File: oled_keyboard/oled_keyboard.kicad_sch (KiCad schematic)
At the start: 115 parts, among them J1 Conn_01x20_Socket, J10 Conn_01x20_Socket, J11 Conn_01x20_Socket, J12 Conn_01x20_Socket, J2 Conn_01x20_Socket, J3 Conn_01x20_Socket, J4 Conn_01x20_Socket, J5 Conn_01x20_Socket, J6 Conn_01x20_Socket, J7 Conn_01x20_Socket, J8 Conn_01x20_Socket, J9 Conn_01x20_Socket, SW1 SW_Push, SW10 SW_Push, SW11 SW_Push, SW12 SW_Push, SW2 SW_Push, SW3 SW_Push, SW4 SW_Push, SW5 SW_Push, SW6 SW_Push, SW7 SW_Push, SW8 SW_Push, SW9 SW_Push, U1 TPS61088RHLR

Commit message: routing in progress
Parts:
- added NT1: NetTie_2, NetTie:NetTie-2_SMD_Pad0.5mm, symbol Device:NetTie_2
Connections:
- net SCLK is gone; now on net SCK: J1.11 (Pin_11), J10.11 (Pin_11), J11.11 (Pin_11), J12.11 (Pin_11), J2.11 (Pin_11), J3.11 (Pin_11), J4.11 (Pin_11), J5.11 (Pin_11), J6.11 (Pin_11), J7.11 (Pin_11), J8.11 (Pin_11), J9.11 (Pin_11)
- net SDIN is gone; now on net MOSI: J1.10 (Pin_10), J10.10 (Pin_10), J11.10 (Pin_10), J12.10 (Pin_10), J2.10 (Pin_10), J3.10 (Pin_10), J4.10 (Pin_10), J5.10 (Pin_10), J6.10 (Pin_10), J7.10 (Pin_10), J8.10 (Pin_10), J9.10 (Pin_10)
- net VUSB is gone; now on net VBUS: L1.1
- net AGND: now also NT1.1; no longer A1.13 (GND), A1.18 (GND), A1.23 (GND), A1.28 (GND), A1.3 (GND), A1.33 (AGND), A1.37 (3V3_EN), A1.38 (GND), A1.8 (GND), C1.2, C10.1, C11.1, C14.2, C15.2, C16.2, C17.2, C18.2, C19.2, C2.2, C20.2, C21.2, C22.2, C23.2, C24.2, C25.2, C26.2, C27.2, C28.2, C29.2, C3.2, C30.2, C31.2, C32.2, C33.2, C34.2, C35.2, C36.2, C37.2, C38.2, C39.2, C4.2, C40.2, C41.2, C42.2, C43.2, C44.2, C45.2, C46.2, C47.2, C48.2, C49.2, C5.2, C50.2, C51.2, C52.2, C53.2, C54.2, C55.2, C56.2, C57.2, C58.2, C59.2, C6.2, R1.2, R10.2, R11.2, R12.2, R13.2, R14.2, R15.2, R16.2, R17.2, R2.2, R3.2, R9.2, U1.21 (PGND), U1.22 (PGND), U1.23 (PGND), U1.24 (PGND), U1.25 (PGND), U1.26 (PGND), U1.27 (PGND), U1.28 (PGND), U1.29 (PGND)
- net COL1: now also A1.5 (GPIO3); no longer A1.6 (GPIO4)
- net COL2: now also A1.4 (GPIO2); no longer A1.7 (GPIO5)
- net COL3: now also A1.2 (GPIO1); no longer A1.9 (GPIO6)
- net CS1: now also A1.6 (GPIO4); no longer A1.10 (GPIO7)
- net CS10: now also A1.17 (GPIO13); no longer A1.26 (GPIO20)
- net CS11: now also A1.19 (GPIO14); no longer A1.27 (GPIO21)
- net CS12: now also A1.20 (GPIO15); no longer A1.29 (GPIO22)
- net CS2: now also A1.7 (GPIO5); no longer A1.11 (GPIO8)
- net CS3: now also A1.9 (GPIO6); no longer A1.12 (GPIO9)
- net CS4: now also A1.10 (GPIO7); no longer A1.14 (GPIO10)
- net CS5: now also A1.11 (GPIO8); no longer A1.15 (GPIO11)
- net CS6: now also A1.12 (GPIO9); no longer A1.16 (GPIO12)
- net CS7: now also A1.14 (GPIO10); no longer A1.17 (GPIO13)
- net CS8: now also A1.15 (GPIO11); no longer A1.19 (GPIO14)
- net CS9: now also A1.16 (GPIO12); no longer A1.20 (GPIO15)
- net DC: now also A1.31 (GPIO26_ADC0)
- net RES: now also A1.32 (GPIO27_ADC1)
- net ROW2: now also A1.27 (GPIO21); no longer A1.2 (GPIO1)
- net ROW3: now also A1.26 (GPIO20); no longer A1.4 (GPIO2)
- net ROW4: now also A1.22 (GPIO17); no longer A1.5 (GPIO3)
- new net GND: A1.13 (GND), A1.18 (GND), A1.23 (GND), A1.28 (GND), A1.3 (GND), A1.33 (AGND), A1.37 (3V3_EN), A1.38 (GND), A1.8 (GND), C1.2, C10.1, C11.1, C14.2, C15.2, C16.2, C17.2, C18.2, C19.2, C2.2, C20.2, C21.2, C22.2, C23.2, C24.2, C25.2, C26.2, C27.2, C28.2, C29.2, C3.2, C30.2, C31.2, C32.2, C33.2, C34.2, C35.2, C36.2, C37.2, C38.2, C39.2, C4.2, C40.2, C41.2, C42.2, C43.2, C44.2, C45.2, C46.2, C47.2, C48.2, C49.2, C5.2, C50.2, C51.2, C52.2, C53.2, C54.2, C55.2, C56.2, C57.2, C58.2, C59.2, C6.2, NT1.2, R1.2, R10.2, R11.2, R12.2, R13.2, R14.2, R15.2, R16.2, R17.2, R2.2, R3.2, R9.2, U1.21 (PGND), U1.22 (PGND), U1.23 (PGND), U1.24 (PGND), U1.25 (PGND), U1.26 (PGND), U1.27 (PGND), U1.28 (PGND), U1.29 (PGND)

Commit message: routing ok. added gitignore
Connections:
- net VOUT is gone; now on net VCC: C14.1, C15.1, C16.1, C6.1, R5.2, U1.14 (VOUT_16), U1.15 (VOUT_14), U1.16 (VOUT_15)
- no-connect marks 0 -> 135

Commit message: added test points
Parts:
- added TP1, TP2, TP3, TP4, TP5, TP6, TP7: TestPoint, TestPoint:TestPoint_Pad_D2.5mm, symbol Connector:TestPoint
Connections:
- net DC: now also TP6.1
- net GND: now also TP3.1
- net MOSI: now also TP4.1
- net RES: now also TP7.1
- net SCK: now also TP5.1
- net VBUS: now also TP2.1
- net VCC: now also TP1.1

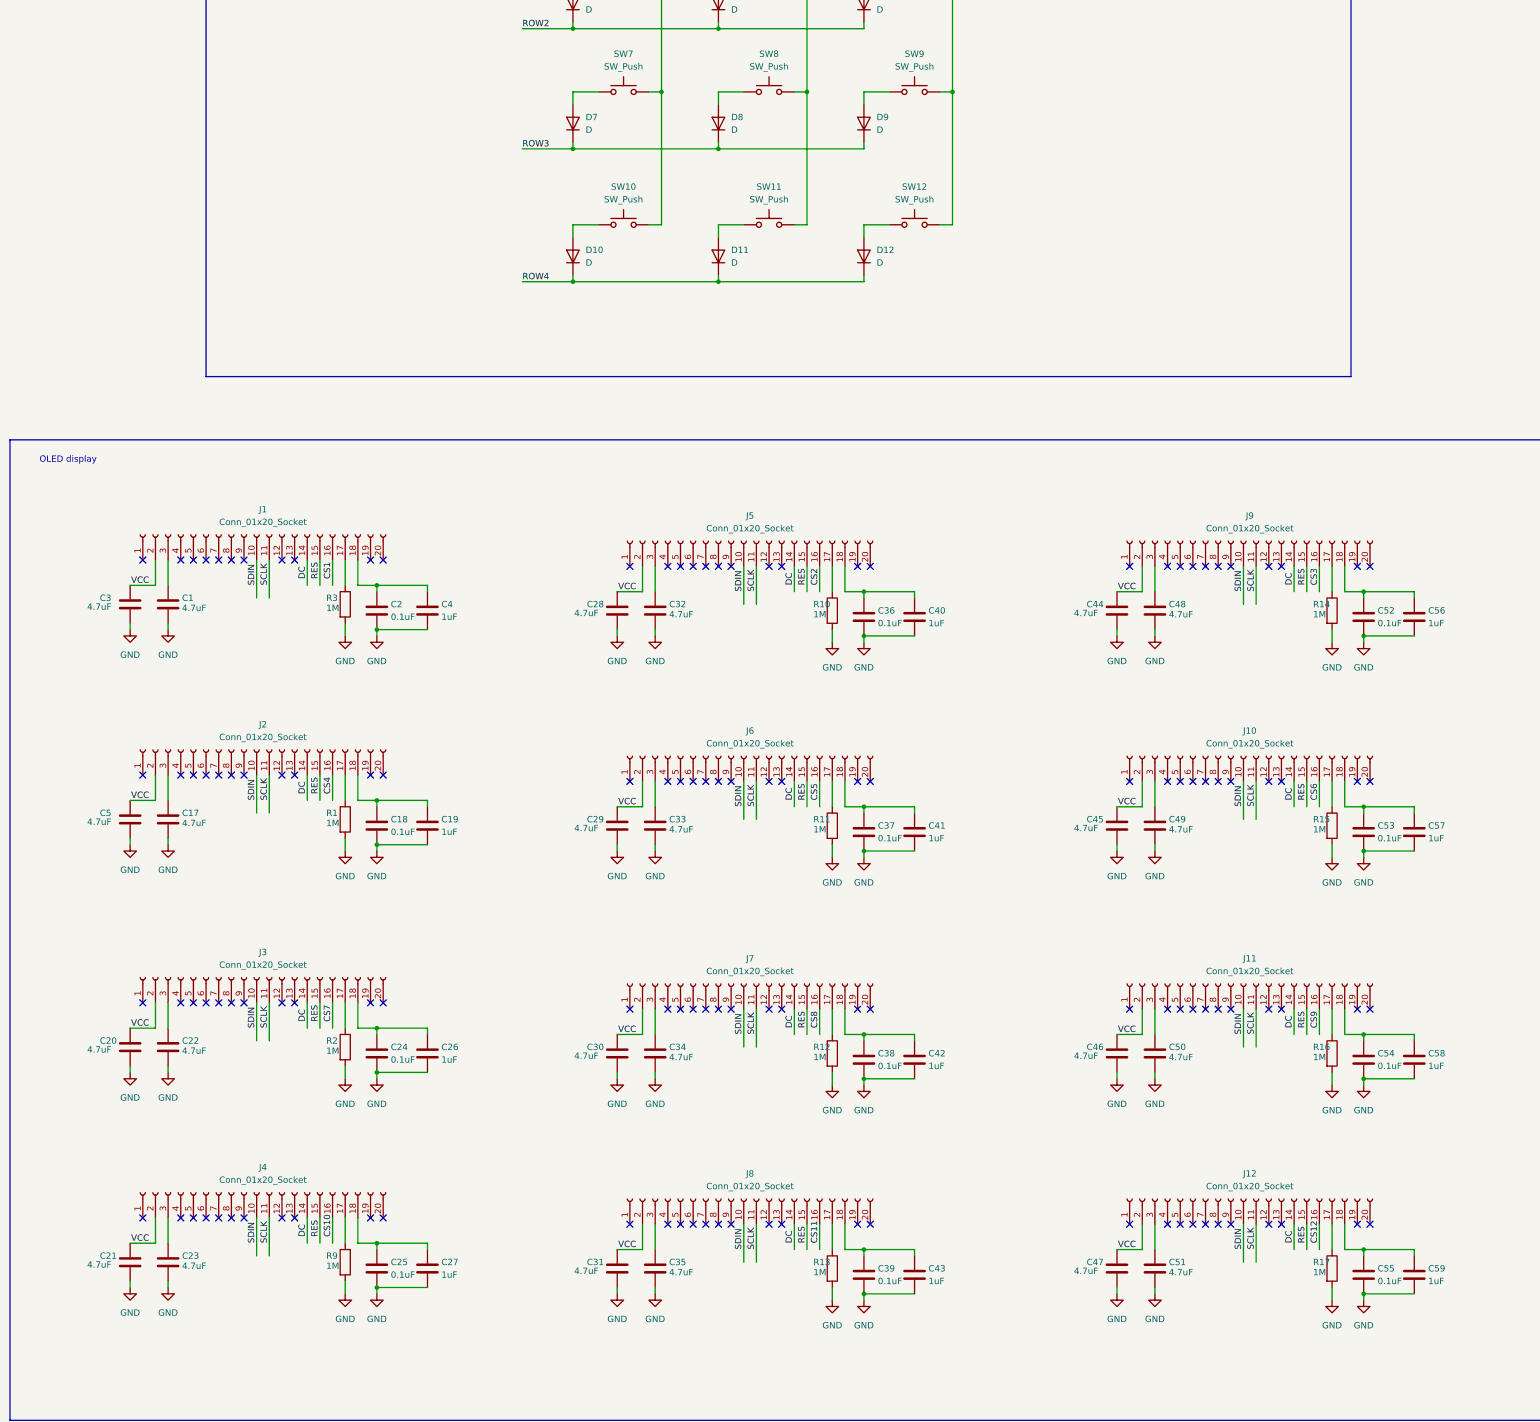
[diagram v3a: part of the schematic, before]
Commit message: chged to 9 oled. fixed pin inversion issue
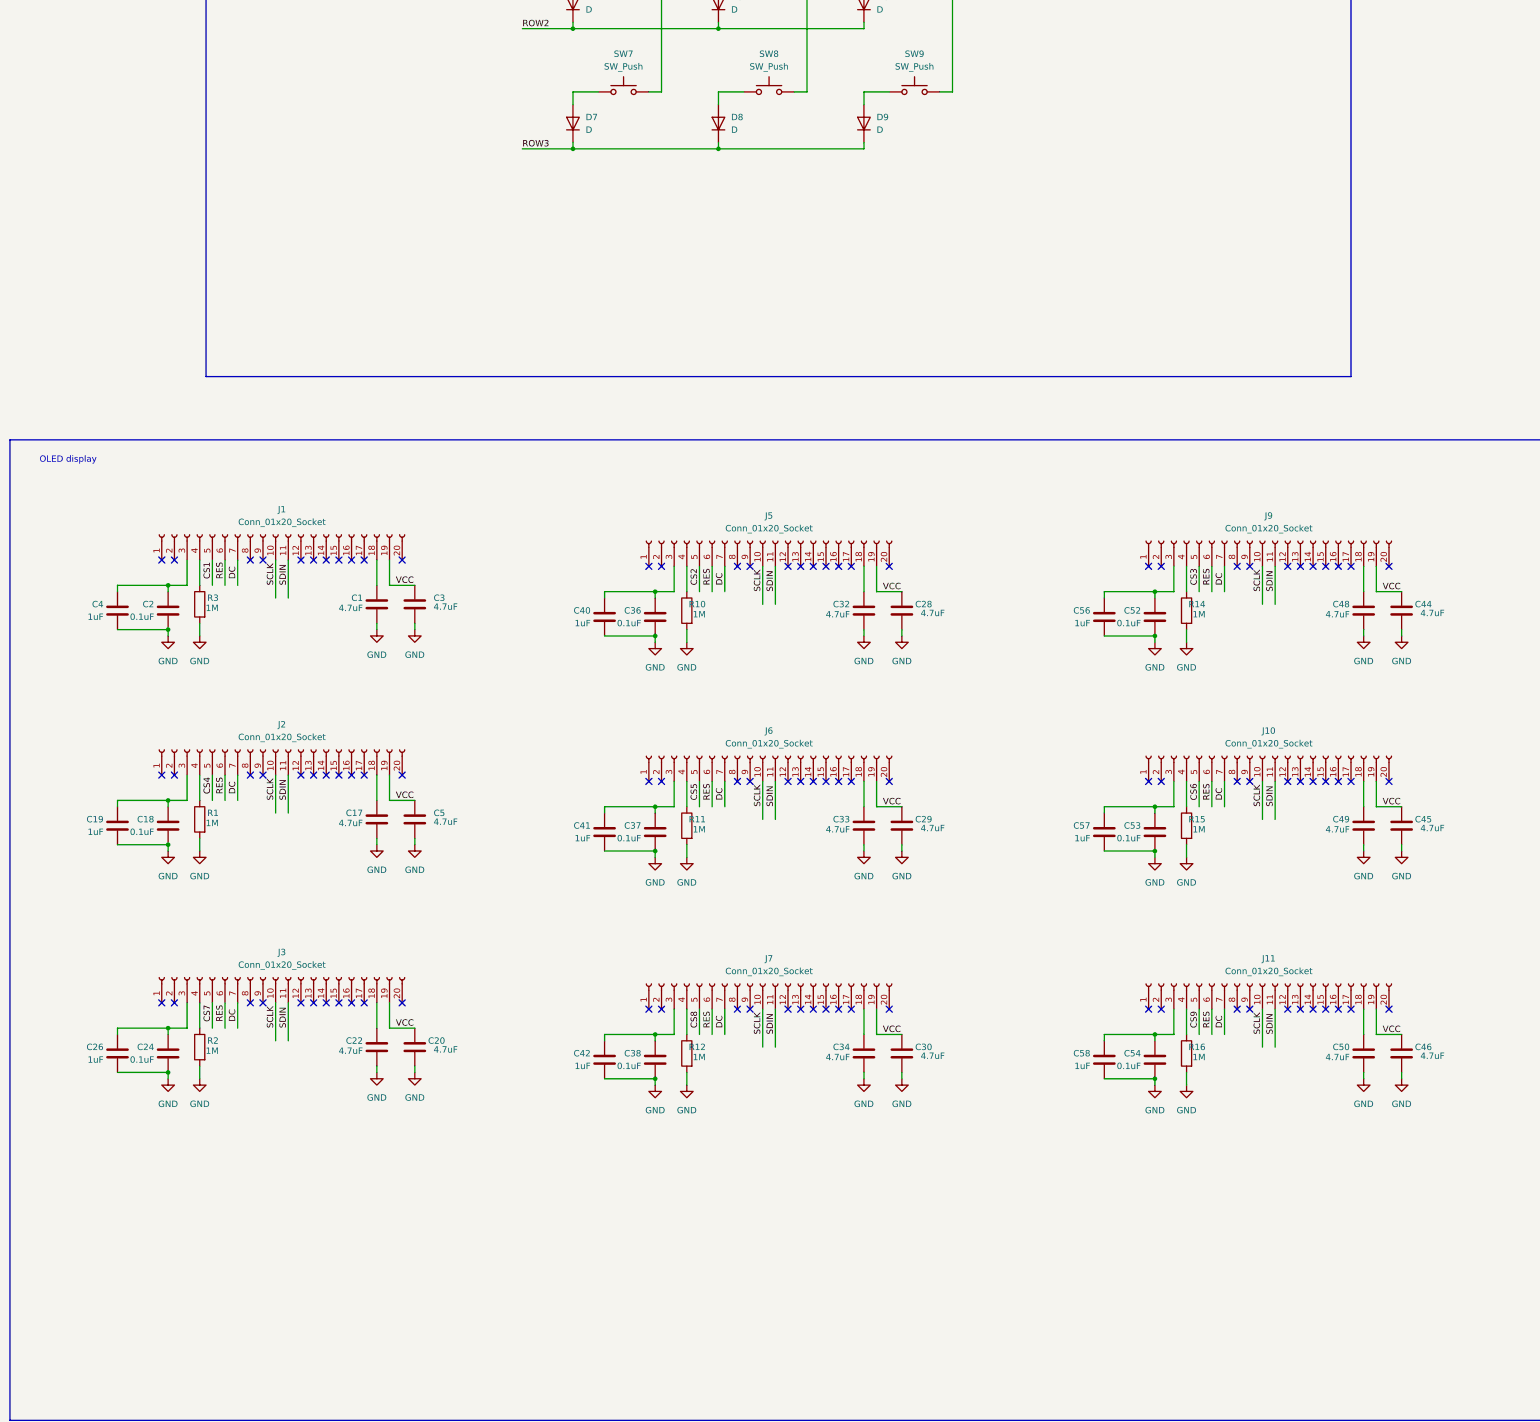
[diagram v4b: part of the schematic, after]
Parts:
- removed C21, C23, C31, C35, C47, C51: 4.7uF, Capacitor_SMD:C_0603_1608Metric, symbol Device:C
- removed C25, C39, C55: 0.1uF, Capacitor_SMD:C_0603_1608Metric, symbol Device:C
- removed C27, C43, C59: 1uF, Capacitor_SMD:C_0603_1608Metric, symbol Device:C
- removed D10, D11, D12: D, Diode_SMD:D_SOD-123F, symbol Device:D
- removed J12, J4, J8: Conn_01x20_Socket, 20p_connector:HRS_TF31-20S-0.5SH_800_, symbol Connector:Conn_01x20_Socket
- removed R13, R17, R9: 1M, Resistor_SMD:R_0603_1608Metric, symbol Device:R
- removed SW10, SW11, SW12: SW_Push, Switch_Keyboard_Kailh:SW_Kailh_Choc_V1V2, symbol Switch:SW_Push
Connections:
- net CS1: now also J1.5 (Pin_5); no longer J1.16 (Pin_16)
- net CS2: now also J5.5 (Pin_5); no longer J5.16 (Pin_16)
- net CS3: now also J9.5 (Pin_5); no longer J9.16 (Pin_16)
- net CS4: now also J2.5 (Pin_5); no longer J2.16 (Pin_16)
- net CS5: now also J6.5 (Pin_5); no longer J6.16 (Pin_16)
- net CS6: now also J10.5 (Pin_5); no longer J10.16 (Pin_16)
- net CS7: now also J3.5 (Pin_5); no longer J3.16 (Pin_16)
- net CS8: now also J7.5 (Pin_5); no longer J7.16 (Pin_16)
- net CS9: now also J11.5 (Pin_5); no longer J11.16 (Pin_16)
- net DC: now also J1.7 (Pin_7), J10.7 (Pin_7), J11.7 (Pin_7), J2.7 (Pin_7), J3.7 (Pin_7), J5.7 (Pin_7), J6.7 (Pin_7), J7.7 (Pin_7), J9.7 (Pin_7); no longer J1.14 (Pin_14), J10.14 (Pin_14), J11.14 (Pin_14), J2.14 (Pin_14), J3.14 (Pin_14), J5.14 (Pin_14), J6.14 (Pin_14), J7.14 (Pin_14), J9.14 (Pin_14)
- net MOSI: now also J1.11 (Pin_11), J10.11 (Pin_11), J11.11 (Pin_11), J2.11 (Pin_11), J3.11 (Pin_11), J5.11 (Pin_11), J6.11 (Pin_11), J7.11 (Pin_11), J9.11 (Pin_11); no longer J1.10 (Pin_10), J10.10 (Pin_10), J11.10 (Pin_10), J2.10 (Pin_10), J3.10 (Pin_10), J5.10 (Pin_10), J6.10 (Pin_10), J7.10 (Pin_10), J9.10 (Pin_10)
- net RES: now also J1.6 (Pin_6), J10.6 (Pin_6), J11.6 (Pin_6), J2.6 (Pin_6), J3.6 (Pin_6), J5.6 (Pin_6), J6.6 (Pin_6), J7.6 (Pin_6), J9.6 (Pin_6); no longer J1.15 (Pin_15), J10.15 (Pin_15), J11.15 (Pin_15), J2.15 (Pin_15), J3.15 (Pin_15), J5.15 (Pin_15), J6.15 (Pin_15), J7.15 (Pin_15), J9.15 (Pin_15)
- net SCK: now also J1.10 (Pin_10), J10.10 (Pin_10), J11.10 (Pin_10), J2.10 (Pin_10), J3.10 (Pin_10), J5.10 (Pin_10), J6.10 (Pin_10), J7.10 (Pin_10), J9.10 (Pin_10); no longer J1.11 (Pin_11), J10.11 (Pin_11), J11.11 (Pin_11), J2.11 (Pin_11), J3.11 (Pin_11), J5.11 (Pin_11), J6.11 (Pin_11), J7.11 (Pin_11), J9.11 (Pin_11)
- net VCC: now also J1.19 (Pin_19), J10.19 (Pin_19), J11.19 (Pin_19), J2.19 (Pin_19), J3.19 (Pin_19), J5.19 (Pin_19), J6.19 (Pin_19), J7.19 (Pin_19), J9.19 (Pin_19); no longer J1.2 (Pin_2), J10.2 (Pin_2), J11.2 (Pin_2), J2.2 (Pin_2), J3.2 (Pin_2), J5.2 (Pin_2), J6.2 (Pin_2), J7.2 (Pin_2), J9.2 (Pin_2)
- net at R16.1: now also J11.4 (Pin_4); no longer J11.17 (Pin_17)
- net at J9.17 (Pin_17): no longer R14.1
- net at C52.1, C56.1: now also J9.3 (Pin_3); no longer J9.18 (Pin_18)
- net at C48.1: now also J9.18 (Pin_18); no longer J9.3 (Pin_3)
- net at J9.4 (Pin_4): now also R14.1
- net at C34.1: now also J7.18 (Pin_18); no longer J7.3 (Pin_3)
- net at C37.1, C41.1: now also J6.3 (Pin_3); no longer J6.18 (Pin_18)
- net at C18.1, C19.1: now also J2.3 (Pin_3); no longer J2.18 (Pin_18)
- net at J2.17 (Pin_17): no longer R1.1
- net at C17.1: now also J2.18 (Pin_18); no longer J2.3 (Pin_3)
- net at J2.4 (Pin_4): now also R1.1
- net at C38.1, C42.1: now also J7.3 (Pin_3); no longer J7.18 (Pin_18)
- net at C36.1, C40.1: now also J5.3 (Pin_3); no longer J5.18 (Pin_18)
- net at C53.1, C57.1: now also J10.3 (Pin_3); no longer J10.18 (Pin_18)
- net at J10.17 (Pin_17): no longer R15.1
- net at C49.1: now also J10.18 (Pin_18); no longer J10.3 (Pin_3)
- net at J10.4 (Pin_4): now also R15.1
- net at R2.1: now also J3.4 (Pin_4); no longer J3.17 (Pin_17)
- net at C24.1, C26.1: now also J3.3 (Pin_3); no longer J3.18 (Pin_18)
- net at C22.1: now also J3.18 (Pin_18); no longer J3.3 (Pin_3)
- net at R10.1: now also J5.4 (Pin_4); no longer J5.17 (Pin_17)
- net at C32.1: now also J5.18 (Pin_18); no longer J5.3 (Pin_3)
- net at C2.1, C4.1: now also J1.3 (Pin_3); no longer J1.18 (Pin_18)
- net at C54.1, C58.1: now also J11.3 (Pin_3); no longer J11.18 (Pin_18)
- net at C50.1: now also J11.18 (Pin_18); no longer J11.3 (Pin_3)
- net at R3.1: now also J1.4 (Pin_4); no longer J1.17 (Pin_17)
- net at C1.1: now also J1.18 (Pin_18); no longer J1.3 (Pin_3)
- net at R11.1: now also J6.4 (Pin_4); no longer J6.17 (Pin_17)
- net at C33.1: now also J6.18 (Pin_18); no longer J6.3 (Pin_3)
- net at J7.17 (Pin_17): no longer R12.1
- net at J7.4 (Pin_4): now also R12.1
- no-connect marks 135 -> 102
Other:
- moved on the sheet: C1, C17, C18, C19, C2, C20, C22, C24, C26, C28, C29, C3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

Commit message: optimized key layout
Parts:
- added C21, C31, C47: 1uF, Capacitor_SMD:C_0603_1608Metric, symbol Device:C
- added C23, C35, C51: 0.1uF, Capacitor_SMD:C_0603_1608Metric, symbol Device:C
- added C25, C27, C39, C43, C55, C59: 4.7uF, Capacitor_SMD:C_0603_1608Metric, symbol Device:C
- added D10, D11, D12: D, Diode_SMD:D_SOD-123F, symbol Device:D
- added J12, J4, J8: Conn_01x20_Socket, 20pin_connector:HRS_TF31-20S-0.5SH_800_, symbol Connector:Conn_01x20_Socket
- added R13, R17, R9: 1M, Resistor_SMD:R_0603_1608Metric, symbol Device:R
- added SW10, SW11, SW12: SW_Push, keyboard_custom:SW_Kailh_Choc_V1V2, symbol Switch:SW_Push
- added TP8: TestPoint, TestPoint:TestPoint_Pad_D2.5mm, symbol Connector:TestPoint
- J1, J10, J11, J2, J3, J5, J6, J7, J9: footprint 20p_connector:HRS_TF31-20S-0.5SH_800_ -> 20pin_connector:HRS_TF31-20S-0.5SH_800_
- SW1, SW2, SW3, SW4, SW5, SW6, SW7, SW8, SW9: footprint Switch_Keyboard_Kailh:SW_Kailh_Choc_V1V2 -> keyboard_custom:SW_Kailh_Choc_V1V2
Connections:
- net COL1: now also SW10.2
- net COL2: now also A1.2 (GPIO1), SW11.2; no longer A1.4 (GPIO2)
- net COL3: now also A1.1 (GPIO0), SW12.2; no longer A1.2 (GPIO1)
- net CS10: now also J4.5 (Pin_5)
- net CS11: now also J8.5 (Pin_5)
- net CS12: now also J12.5 (Pin_5)
- net DC: now also J12.7 (Pin_7), J4.7 (Pin_7), J8.7 (Pin_7)
- net GND: now also C21.2, C23.2, C25.2, C27.2, C31.2, C35.2, C39.2, C43.2, C47.2, C51.2, C55.2, C59.2, R13.2, R17.2, R9.2, TP8.1
- net MOSI: now also J12.11 (Pin_11), J4.11 (Pin_11), J8.11 (Pin_11)
- net RES: now also J12.6 (Pin_6), J4.6 (Pin_6), J8.6 (Pin_6)
- net ROW1: now also A1.4 (GPIO2); no longer A1.1 (GPIO0)
- net ROW4: now also D10.1 (K), D11.1 (K), D12.1 (K)
- net SCK: now also J12.10 (Pin_10), J4.10 (Pin_10), J8.10 (Pin_10)
- net VCC: now also C27.1, C43.1, C59.1, J12.19 (Pin_19), J4.19 (Pin_19), J8.19 (Pin_19)
- new net: C21.1, C23.1, J4.3 (Pin_3)
- new net: D12.2 (A), SW12.1
- new net: C25.1, J4.18 (Pin_18)
- new net: J4.4 (Pin_4), R9.1
- new net: D11.2 (A), SW11.1
- new net: J12.4 (Pin_4), R17.1
- new net: D10.2 (A), SW10.1
- new net: C31.1, C35.1, J8.3 (Pin_3)
- new net: C39.1, J8.18 (Pin_18)
- new net: J8.4 (Pin_4), R13.1
- new net: C55.1, J12.18 (Pin_18)
- new net: C47.1, C51.1, J12.3 (Pin_3)
- no-connect marks 102 -> 135

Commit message: v3.0
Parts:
- added R18, R19: 33R, Resistor_SMD:R_0603_1608Metric, symbol Device:R
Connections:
- net MOSI: now also R19.2; no longer J1.11 (Pin_11), J10.11 (Pin_11), J11.11 (Pin_11), J12.11 (Pin_11), J2.11 (Pin_11), J3.11 (Pin_11), J4.11 (Pin_11), J5.11 (Pin_11), J6.11 (Pin_11), J7.11 (Pin_11), J8.11 (Pin_11), J9.11 (Pin_11)
- net SCK: now also R18.2; no longer J1.10 (Pin_10), J10.10 (Pin_10), J11.10 (Pin_10), J12.10 (Pin_10), J2.10 (Pin_10), J3.10 (Pin_10), J4.10 (Pin_10), J5.10 (Pin_10), J6.10 (Pin_10), J7.10 (Pin_10), J8.10 (Pin_10), J9.10 (Pin_10)
- new net SCLK: J1.10 (Pin_10), J10.10 (Pin_10), J11.10 (Pin_10), J12.10 (Pin_10), J2.10 (Pin_10), J3.10 (Pin_10), J4.10 (Pin_10), J5.10 (Pin_10), J6.10 (Pin_10), J7.10 (Pin_10), J8.10 (Pin_10), J9.10 (Pin_10), R18.1
- new net SDIN: J1.11 (Pin_11), J10.11 (Pin_11), J11.11 (Pin_11), J12.11 (Pin_11), J2.11 (Pin_11), J3.11 (Pin_11), J4.11 (Pin_11), J5.11 (Pin_11), J6.11 (Pin_11), J7.11 (Pin_11), J8.11 (Pin_11), J9.11 (Pin_11), R19.1
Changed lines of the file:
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@@
 	(wire
 		(pts
-			(xy 492.76 165.1) (xy 513.08 165.1)
+			(xy 492.76 165.1) (xy 505.46 165.1)
 		)
 		(stroke
@@
 	(wire
 		(pts
+			(xy 513.08 162.56) (xy 520.7 162.56)
+		)
+		(stroke
+			(width 0)
+			(type default)
+		)
+	)
+	(wire
+		(pts
 			(xy 144.78 214.63) (xy 144.78 213.36)
 		)
@@
 	(wire
 		(pts
+			(xy 513.08 165.1) (xy 520.7 165.1)
+		)
+		(stroke
+			(width 0)
+			(type default)
+		)
+	)
+	(wire
+		(pts
 			(xy 63.5 347.98) (xy 63.5 342.9)
 		)
@@
 	(wire
 		(pts
-			(xy 492.76 162.56) (xy 513.08 162.56)
+			(xy 492.76 162.56) (xy 505.46 162.56)
 		)
 		(stroke
@@
 	)
 	(label "SCK"
-		(at 499.11 162.56 0)
+		(at 495.3 162.56 0)
 		(effects
 			(font
@@
 	)
 	(label "SCLK"
-		(at 513.08 162.56 180)
+		(at 520.7 162.56 180)
 		(effects
 			(font
@@
 	)
 	(label "SDIN"
-		(at 513.08 165.1 180)
+		(at 520.7 165.1 180)
 		(effects
 			(font
@@
 	)
 	(label "MOSI"
-		(at 499.11 165.1 0)
+		(at 494.03 165.1 0)
 		(effects
 			(font
@@
 	)
 	(symbol
+		(lib_id "Device:R")
+		(at 509.27 162.56 270)
+		(unit 1)
+		(exclude_from_sim no)
+		(in_bom yes)
+		(on_board yes)
+		(dnp no)
+		(property "Reference" "R18"
+			(at 505.714 160.528 90)
+			(effects
+				(font
+					(size 1.27 1.27)
+				)
+				(justify left)
+			)
+		)
+		(property "Value" "33R"
+			(at 509.778 160.528 90)
+			(effects
+				(font
+					(size 1.27 1.27)
+				)
+				(justify left)
+			)
+		)
+		(property "Footprint" "Resistor_SMD:R_0603_1608Metric"
+			(at 509.27 160.782 90)
+			(effects
+				(font
+					(size 1.27 1.27)
+				)
+				(hide yes)
+			)
+		)
+		(property "Datasheet" "~"
+			(at 509.27 162.56 0)
+			(effects
+				(font
+					(size 1.27 1.27)
+				)
+				(hide yes)
+			)
+		)
+		(property "Description" "Resistor"
+			(at 509.27 162.56 0)
+			(effects
+				(font
+					(size 1.27 1.27)
+				)
+				(hide yes)
+			)
+		)
+		(pin "1"
+		)
+		(pin "2"
+		)
+		(instances
+			(project "oled_keyboard"
+				(path "/93cb1d80-50e0-4756-95e4-c1195d62fad8"
+					(reference "R18")
+					(unit 1)
+				)
+			)
+		)
+	)
+	(symbol
 		(lib_id "Device:NetTie_2")
 		(at 518.16 336.55 180)
@@
 					(unit 1)
 				)
+			)
+		)
+	)
+	(symbol
+		(lib_id "Device:R")
+		(at 509.27 165.1 270)
+		(unit 1)
+		(exclude_from_sim no)
+		(in_bom yes)
+		(on_board yes)
+		(dnp no)
+		(property "Reference" "R19"
+			(at 505.46 167.64 90)
+			(effects
+				(font
+					(size 1.27 1.27)
+				)
+				(justify left)
+			)
+		)
+		(property "Value" "33R"
+			(at 509.27 167.64 90)
+			(effects
+				(font
+					(size 1.27 1.27)
+				)
+				(justify left)
+			)
+		)
+		(property "Footprint" "Resistor_SMD:R_0603_1608Metric"
+			(at 509.27 163.322 90)
+			(effects
+				(font
+					(size 1.27 1.27)
+				)
+				(hide yes)
+			)
+		)
+		(property "Datasheet" "~"
+			(at 509.27 165.1 0)
+			(effects
+				(font
+					(size 1.27 1.27)
+				)
+				(hide yes)
+			)
+		)
+		(property "Description" "Resistor"
+			(at 509.27 165.1 0)
+			(effects
+				(font
+					(size 1.27 1.27)
+				)
+				(hide yes)
+			)
+		)
+		(pin "1"
+		)
+		(pin "2"
+		)
+		(instances
+			(project "oled_keyboard"
+				(path "/93cb1d80-50e0-4756-95e4-c1195d62fad8"
+					(reference "R19")
+					(unit 1)
+				)
